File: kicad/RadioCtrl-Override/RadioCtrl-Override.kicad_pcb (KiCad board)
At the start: 2 copper layers, 75 x 50 mm, 20 parts, among them J1 FW/BK/CON, J2 LF/RI/CON, J3 PJ-002AH, J5 HM10, J6 WRITER, Q1 2SC1815, Q2 2SC1815, Q3 2SC1815, Q4 2SC1815, U1 PIC16F1827-E/P

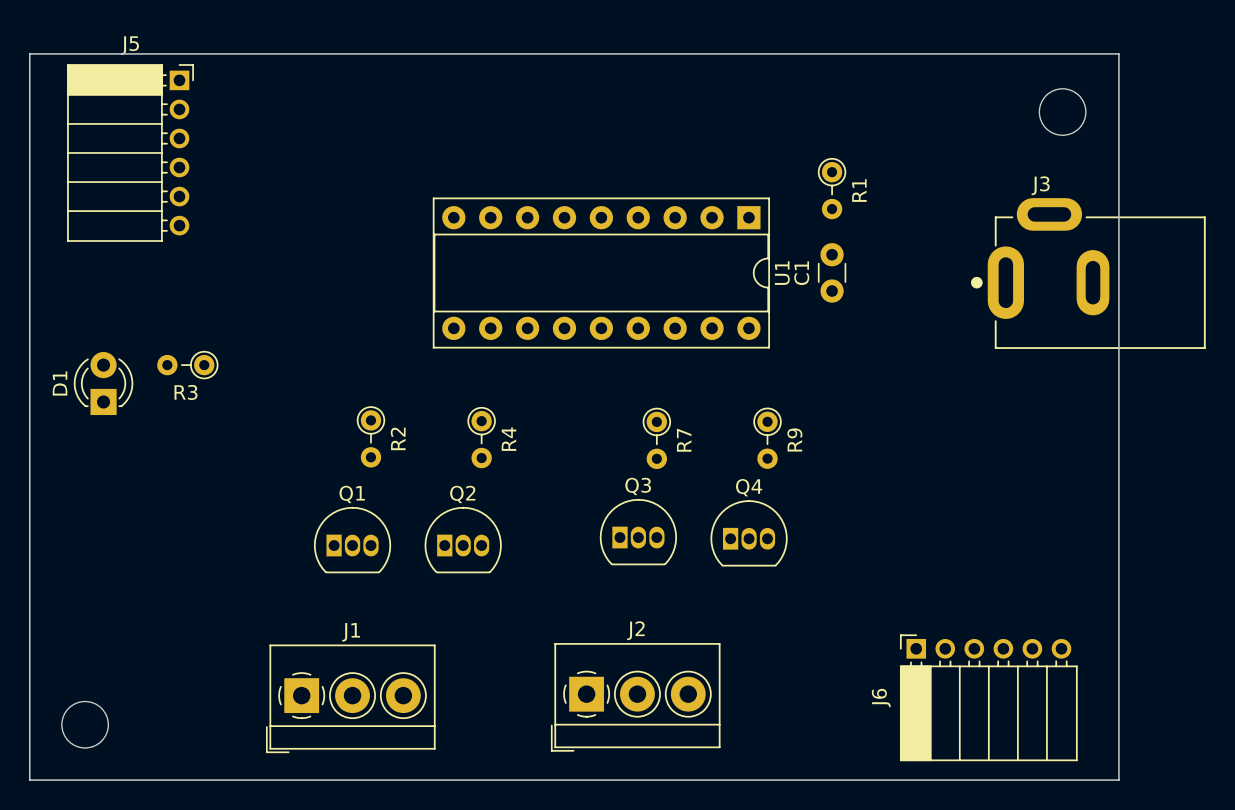
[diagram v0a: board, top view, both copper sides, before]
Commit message: 配線を実装
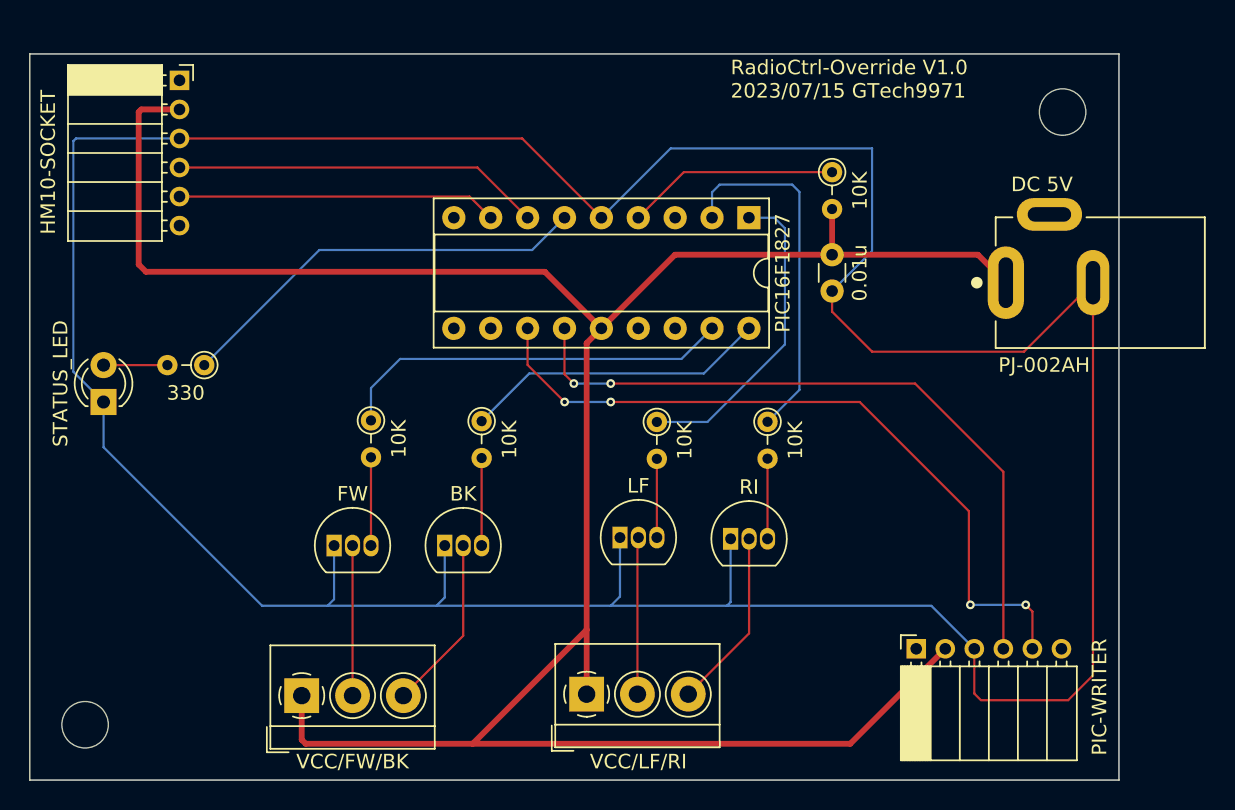
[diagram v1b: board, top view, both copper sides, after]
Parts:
- DC 5V: renamed from J3
- renumbered C1 to 0.01u, R1 to 10K, R7 to 10K, R4 to 10K, R2 to 10K, R9 to 10K, R3 to 330, Q2 to BK, Q1 to FW, J5 to HM10-SOCKET, Q3 to LF, J6 to PIC-WRITER, U1 to PIC16F1827, Q4 to RI, D1 to STATUS_LED, J1 to VCC/FW/BK, J2 to VCC/LF/RI
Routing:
- net GND: track 0.00 -> 238.0 mm
- net VCC: track 0.00 -> 167.8 mm
- net ICSPCLK: track 0.00 -> 50.6 mm, vias 0 -> 4
- net ICSPDAT: track 0.00 -> 48.3 mm, vias 0 -> 2
- net LED_STATUS: track 0.00 -> 29.0 mm
- net FW_IN: track 0.00 -> 27.4 mm
- net HM10_TX: track 0.00 -> 25.4 mm
- net RI_IN: track 0.00 -> 24.9 mm
- net HM10_RX: track 0.00 -> 22.0 mm
- net LF_IN: track 0.00 -> 21.8 mm
- net BK_IN: track 0.00 -> 21.1 mm
- net Net-(R1-Pad1): track 0.00 -> 14.6 mm
- net RI_GND: track 0.00 -> 12.4 mm
- net BK_GND: track 0.00 -> 12.0 mm
- net LF_GND: track 0.00 -> 10.8 mm
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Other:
- board text added: "BK/FW/VCC"
- board text added: "CLK"
- board text added: "DAT"
- board text added: "GND"
- board text added: "PJ-002AH"
- board text added: "RI/LF/VCC"
- board text added: "RadioCtrl-Override V1.0 2023/07/15 GTech9971"
- board text added: "VCC"

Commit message: ベタグラウンド、ビア追加
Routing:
- net GND: vias 0 -> 23
- added copper zone on B.Cu, net GND
- added copper zone on F.Cu, net GND

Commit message: FusionPCBに注文
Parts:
- renumbered STATUS_LED to STATUS-LED
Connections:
- 10K pad 1: Net-(R1-Pad1) -> MCLR
- PIC-WRITER pad 1: unconnected-(J6-Pad1) -> MCLR
- PIC16F1827 pad 4: Net-(R1-Pad1) -> MCLR
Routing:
- net MCLR: track 0.00 -> 50.6 mm, vias 0 -> 2
- net Net-(R1-Pad1): track 14.6 -> 0.00 mm
- net GND: vias 23 -> 21

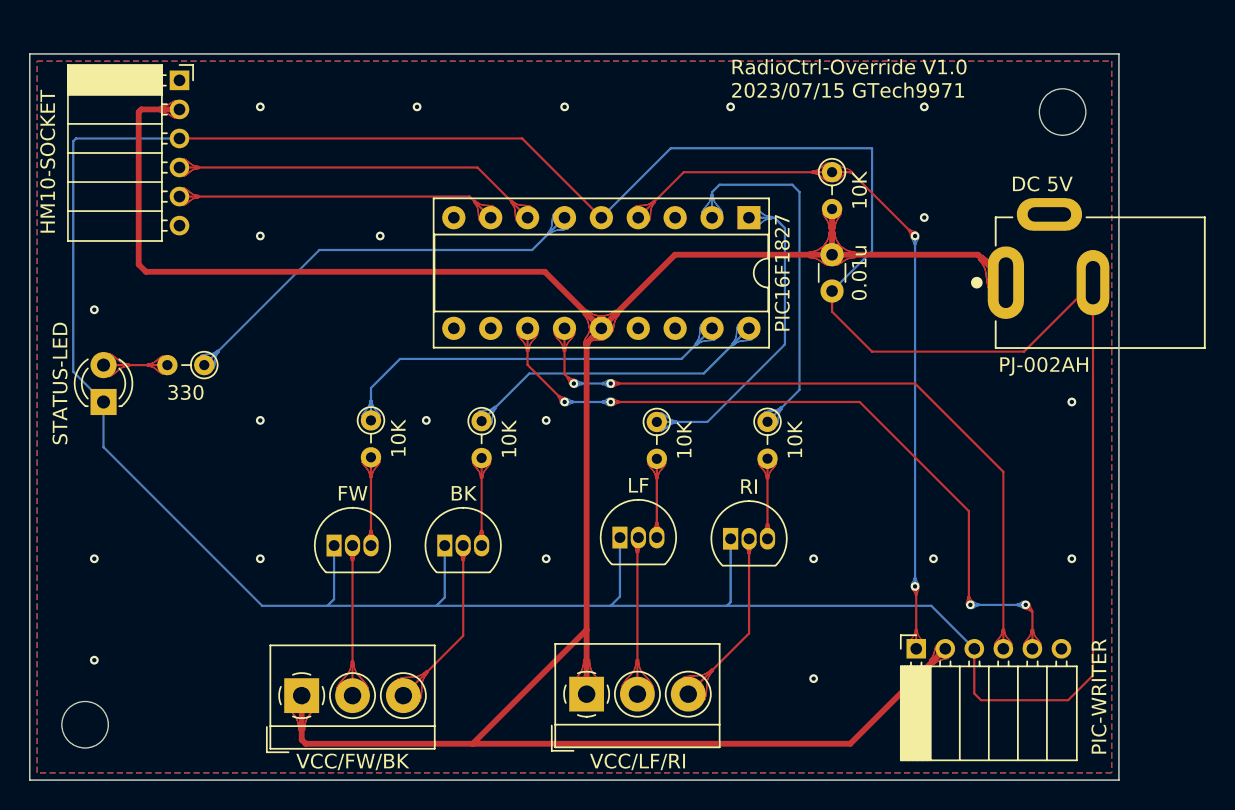
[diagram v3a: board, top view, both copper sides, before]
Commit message: シンボルのサイズが異なっていたため修正
コネクタとターミナル、トランジスタのサイズを変更
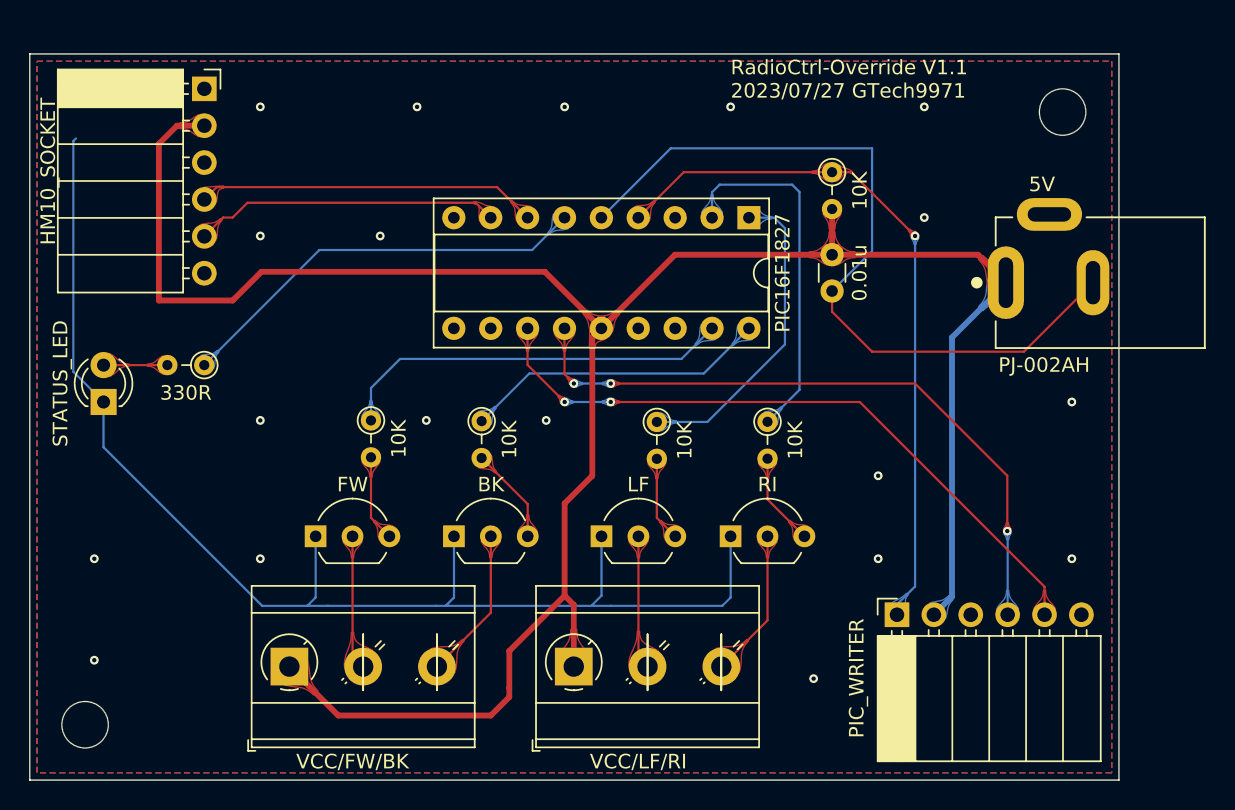
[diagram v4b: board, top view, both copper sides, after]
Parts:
- 5V: renamed from DC 5V
- BK, FW, LF, RI: footprint Package_TO_SOT_THT:TO-92_Inline -> Package_TO_SOT_THT:TO-92_Inline_Wide
- HM10_SOCKET: renamed from HM10-SOCKET; footprint Connector_PinSocket_2.00mm:PinSocket_1x06_P2.00mm_Horizontal -> Connector_PinSocket_2.54mm:PinSocket_1x06_P2.54mm_Horizontal
- PIC_WRITER: renamed from PIC-WRITER; footprint Connector_PinSocket_2.00mm:PinSocket_1x06_P2.00mm_Horizontal -> Connector_PinSocket_2.54mm:PinSocket_1x06_P2.54mm_Horizontal
- VCC/FW/BK: value FW/BK/CON -> VCC/FW/BK; footprint TerminalBlock_4Ucon:TerminalBlock_4Ucon_1x03_P3.50mm_Horizontal -> TerminalBlock_MetzConnect:TerminalBlock_MetzConnect_Type073_RT02603HBLU_1x03_P5.08mm_Horizontal
- VCC/LF/RI: footprint TerminalBlock_4Ucon:TerminalBlock_4Ucon_1x03_P3.50mm_Horizontal -> TerminalBlock_MetzConnect:TerminalBlock_MetzConnect_Type073_RT02603HBLU_1x03_P5.08mm_Horizontal
- moved PIC_WRITER 2.69 mm to (189.7, 118.6)
- moved VCC/FW/BK 2.17 mm to (147.9, 122.2)
- moved VCC/LF/RI 2.09 mm to (167.5, 122.2)
- moved HM10_SOCKET 1.81 mm to (142.0, 82.4)
- moved FW 1.42 mm to (149.7, 113.2)
- moved LF 1.27 mm to (169.4, 113.2)
- moved BK 0.90 mm to (159.2, 113.2)
- moved RI 0.17 mm to (178.3, 113.2)
- renumbered 330 to 330R, STATUS-LED to STATUS_LED
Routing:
- net GND: track 238.0 -> 143.5 mm, vias 21 -> 19
- net VCC: track 167.8 -> 157.0 mm
- net ICSPCLK: track 50.6 -> 46.4 mm, vias 4 -> 2
- net ICSPDAT: track 48.3 -> 46.1 mm, vias 2 -> 3
- net RI_GND: track 12.4 -> 10.3 mm
- net HM10_TX: track 25.4 -> 23.5 mm
- net MCLR: track 50.6 -> 48.8 mm, vias 2 -> 1
- net LF_GND: track 10.8 -> 9.23 mm
- net BK_GND: track 12.0 -> 10.5 mm
- net FW_GND: track 10.3 -> 9.27 mm
- net HM10_RX: track 22.0 -> 21.1 mm
- net Net-(Q4-Pad3): track 5.52 -> 6.40 mm
- net Net-(Q2-Pad3): track 6.02 -> 6.71 mm
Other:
- board text added: "RadioCtrl-Override V1.1 2023/07/27 GTech9971"
- board text removed: "RadioCtrl-Override V1.0 2023/07/15 GTech9971"

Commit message: 基盤の内容を修正
ターミナルのVCCをGNDに変更
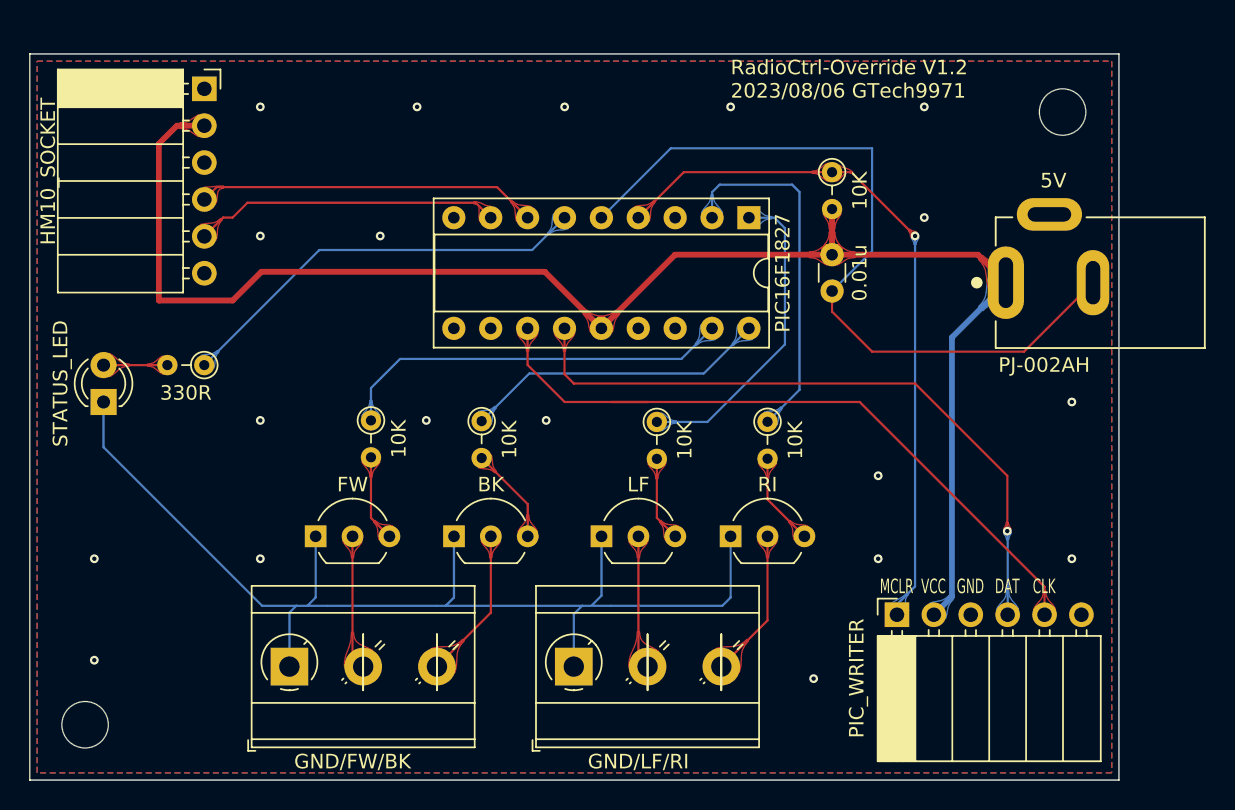
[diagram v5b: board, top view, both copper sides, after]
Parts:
- GND/FW/BK: renamed from VCC/FW/BK; value VCC/FW/BK -> FW/BK/CON
- renumbered VCC/LF/RI to GND/LF/RI, 5V to PJ-002AH
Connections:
- GND/FW/BK pad 1: VCC -> GND
- GND/LF/RI pad 1: VCC -> GND
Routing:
- net VCC: track 157.0 -> 106.7 mm
- net GND: track 143.5 -> 133.2 mm
- net ICSPCLK: track 46.4 -> 48.9 mm, vias 2 -> 0
- net ICSPDAT: vias 3 -> 1
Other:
- board text added: "5V"
- board text added: "BK/FW/GND"
- board text added: "MCLR"
- board text added: "RI/LF/GND"
- board text added: "RadioCtrl-Override V1.2 2023/08/06 GTech9971"
- board text removed: "BK/FW/VCC"
- board text removed: "PJ-002AH"
- board text removed: "RI/LF/VCC"
- board text removed: "RadioCtrl-Override V1.1 2023/07/27 GTech9971"
